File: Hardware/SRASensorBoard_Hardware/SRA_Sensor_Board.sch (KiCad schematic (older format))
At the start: 4 parts

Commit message: Added Okis to board
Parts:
- added C? (x4): CP1, symbol Device:CP1
- added C? (x2): C, symbol Device:C
- added D? (x2): LED, symbol Device:LED
- added J? (x2): Test_Point, symbol MRDT_Connectors:Test_Point
- added R? (x2): R, symbol Device:R
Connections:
- net at U?.1 (IN): now also C?.1 (x2)
- net at U?.2 (GND): now also C?.2, C?.2, C?.2 (x2)
- net at U?.3 (OUT): now also C?.1, C?.1, J?.1, R?.2 (x2)
- new net: D?.2 (A), R?.1 (x2)
- new net GND: D?.1 (K), D?.1 (K)
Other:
- moved on the sheet: Conn?A, Conn?B, U?

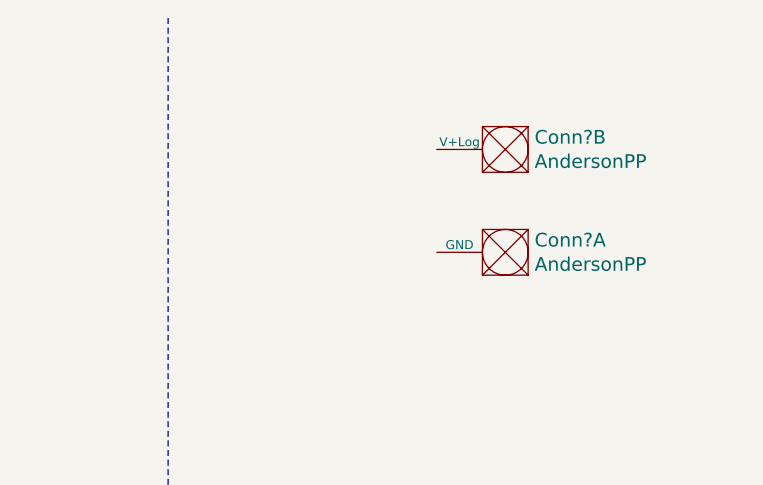
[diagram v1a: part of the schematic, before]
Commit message: Connected andersons 12v and gnd
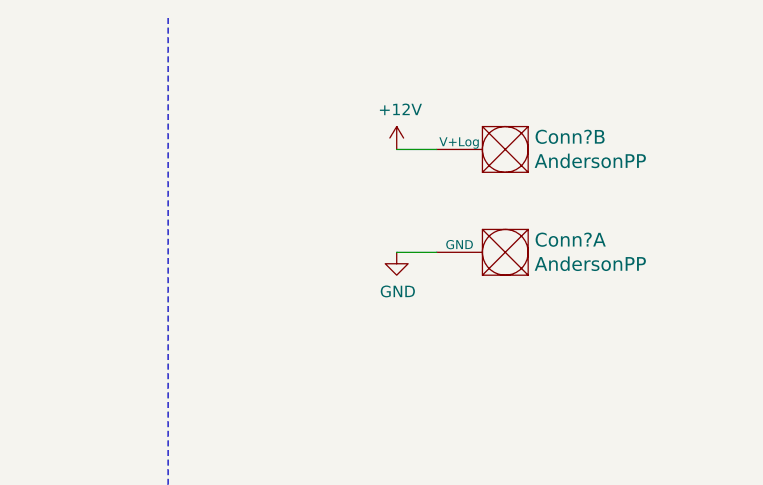
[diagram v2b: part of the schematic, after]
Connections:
- net GND: now also Conn?.1 (GND)
- net +12V: now reaches Conn?.2 (V+Log)
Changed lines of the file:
@@
 Wire Wire Line
 	9700 5225 10000 5225
+$Comp
+L power:+12V #PWR?
+U 1 1 615F977E
+P 9700 1050
+F 0 "#PWR?" H 9700 900 50  0001 C CNN
+F 1 "+12V" H 9715 1223 50  0000 C CNN
+F 2 "" H 9700 1050 50  0001 C CNN
+F 3 "" H 9700 1050 50  0001 C CNN
+	1    9700 1050
+	1    0    0    -1
+$EndComp
+$Comp
+L power:GND #PWR?
+U 1 1 615FA471
+P 9700 1500
+F 0 "#PWR?" H 9700 1250 50  0001 C CNN
+F 1 "GND" H 9705 1327 50  0000 C CNN
+F 2 "" H 9700 1500 50  0001 C CNN
+F 3 "" H 9700 1500 50  0001 C CNN
+	1    9700 1500
+	1    0    0    -1
+$EndComp
+Wire Wire Line
+	9700 1500 9875 1500
+Wire Wire Line
+	9875 1050 9700 1050
 $EndSCHEMATC

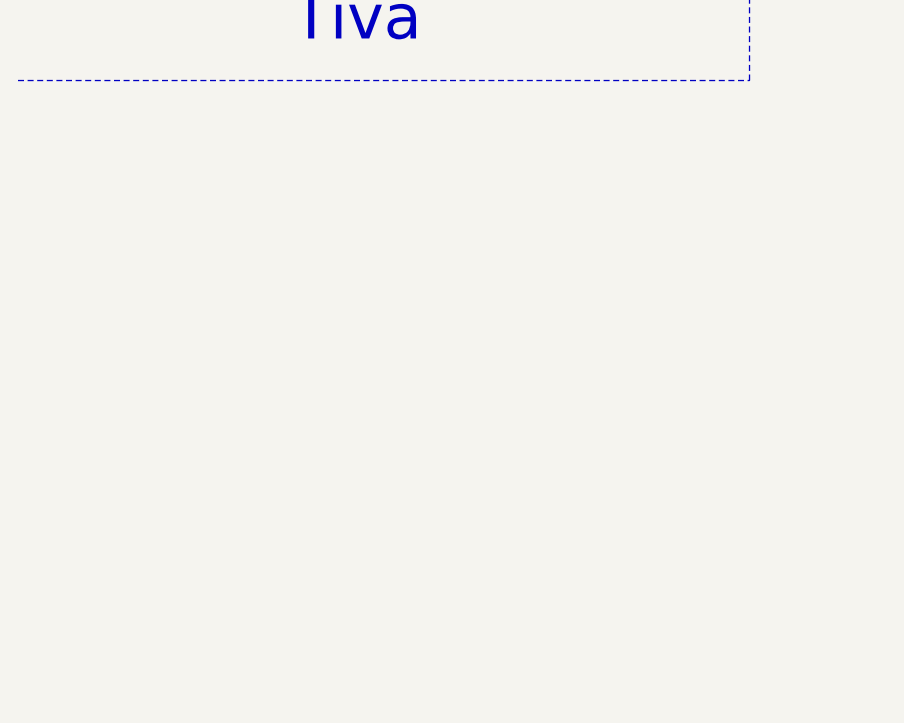
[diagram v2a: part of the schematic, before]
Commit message: Griffin_Buschjost_O2_Sensor
Copied in O2 Sensor from last year and added global labels to TIVA in pin 3 and 4 for the TIVA O2 RX and TX
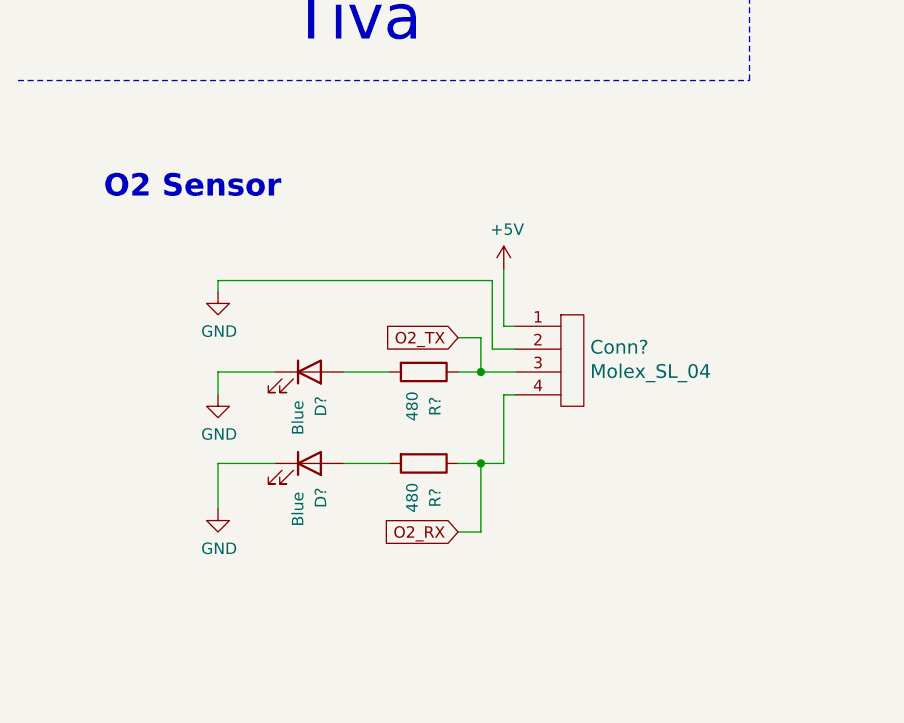
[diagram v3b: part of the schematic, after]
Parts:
- added Conn?: Molex_SL_04, symbol MRDT_Connectors:Molex_SL_04
- added D? (x2): Blue, symbol Device:LED
- added R? (x2): 480, symbol Device:R
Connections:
- net GND: now also Conn?.2, D?.1 (K), D?.1 (K)
- new net: D?.2 (A), R?.2 (x2)
- new net +5V: Conn?.1
- new net O2_RX: Conn?.4, R?.1
- new net O2_TX: Conn?.3, R?.1
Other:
- note added: "O2 Sensor"
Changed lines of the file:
@@
 Wire Wire Line
 	9875 1050 9700 1050
+$Comp
+L MRDT_Connectors:Molex_SL_04 Conn?
+U 1 1 615E28BA
+P 2850 4900
+F 0 "Conn?" H 2978 5158 60  0000 L CNN
+F 1 "Molex_SL_04" H 2978 5052 60  0000 L CNN
+F 2 "" H 2850 4900 60  0001 C CNN
+F 3 "" H 2850 4900 60  0001 C CNN
+	1    2850 4900
+	1    0    0    -1
+$EndComp
+$Comp
+L power:+5V #PWR?
+U 1 1 615E34E6
+P 2600 4300
+F 0 "#PWR?" H 2600 4150 50  0001 C CNN
+F 1 "+5V" H 2615 4473 50  0000 C CNN
+F 2 "" H 2600 4300 50  0001 C CNN
+F 3 "" H 2600 4300 50  0001 C CNN
+	1    2600 4300
+	1    0    0    -1
+$EndComp
+$Comp
+L power:GND #PWR?
+U 1 1 615E3C3C
+P 1350 4400
+F 0 "#PWR?" H 1350 4150 50  0001 C CNN
+F 1 "GND" H 1355 4227 50  0000 C CNN
+F 2 "" H 1350 4400 50  0001 C CNN
+F 3 "" H 1350 4400 50  0001 C CNN
+	1    1350 4400
+	1    0    0    -1
+$EndComp
+$Comp
+L Device:R R?
+U 1 1 615E564A
+P 2250 4750
+F 0 "R?" H 2400 4800 50  0000 C CNN
+F 1 "480" H 2400 4700 50  0000 C CNN
+F 2 "" V 2180 4750 50  0001 C CNN
+F 3 "~" H 2250 4750 50  0001 C CNN
+	1    2250 4750
+	0    1    1    0
+$EndComp
+$Comp
+L Device:R R?
+U 1 1 615E6832
+P 2250 5150
+F 0 "R?" H 2400 5200 50  0000 C CNN
+F 1 "480" H 2400 5100 50  0000 C CNN
+F 2 "" V 2180 5150 50  0001 C CNN
+F 3 "~" H 2250 5150 50  0001 C CNN
+	1    2250 5150
+	0    1    1    0
+$EndComp
+Wire Wire Line
+	2650 4550 2600 4550
+Wire Wire Line
+	2600 4550 2600 4300
+Wire Wire Line
+	2650 4650 2550 4650
+Wire Wire Line
+	2550 4650 2550 4350
+Wire Wire Line
+	2400 4750 2500 4750
+Wire Wire Line
+	2650 4850 2600 4850
+Wire Wire Line
+	2600 4850 2600 5150
+Wire Wire Line
+	2600 5150 2500 5150
+Connection ~ 2500 5150
+Wire Wire Line
+	2500 5150 2400 5150
+Wire Wire Line
+	2500 4750 2500 4600
+Wire Wire Line
+	2500 4600 2400 4600
+Connection ~ 2500 4750
+Wire Wire Line
+	2500 4750 2650 4750
+Text GLabel 2400 4600 0    50   Input ~ 0
+O2_TX
+Wire Wire Line
+	2100 4750 1900 4750
+Wire Wire Line
+	2100 5150 1900 5150
+$Comp
+L Device:LED D?
+U 1 1 615F2521
+P 1750 4750
+F 0 "D?" V 1800 4600 50  0000 C CNN
+F 1 "Blue" V 1700 4550 50  0000 C CNN
+F 2 "" H 1750 4750 50  0001 C CNN
+F 3 "~" H 1750 4750 50  0001 C CNN
+	1    1750 4750
+	1    0    0    -1
+$EndComp
+$Comp
+L Device:LED D?
+U 1 1 615F31B4
+P 1750 5150
+F 0 "D?" V 1800 5000 50  0000 C CNN
+F 1 "Blue" V 1700 4950 50  0000 C CNN
+F 2 "" H 1750 5150 50  0001 C CNN
+F 3 "~" H 1750 5150 50  0001 C CNN
+	1    1750 5150
+	1    0    0    -1
+$EndComp
+Wire Wire Line
+	1350 4750 1600 4750
+Wire Wire Line
+	1600 5150 1350 5150
+Wire Wire Line
+	1350 5150 1350 5350
+$Comp
+L power:GND #PWR?
+U 1 1 615F9848
+P 1350 4850
+F 0 "#PWR?" H 1350 4600 50  0001 C CNN
+F 1 "GND" H 1355 4677 50  0000 C CNN
+F 2 "" H 1350 4850 50  0001 C CNN
+F 3 "" H 1350 4850 50  0001 C CNN
+	1    1350 4850
+	1    0    0    -1
+$EndComp
+$Comp
+L power:GND #PWR?
+U 1 1 615FAB5A
+P 1350 5350
+F 0 "#PWR?" H 1350 5100 50  0001 C CNN
+F 1 "GND" H 1355 5177 50  0000 C CNN
+F 2 "" H 1350 5350 50  0001 C CNN
+F 3 "" H 1350 5350 50  0001 C CNN
+	1    1350 5350
+	1    0    0    -1
+$EndComp
+Wire Wire Line
+	1350 4750 1350 4850
+Wire Wire Line
+	2500 5450 2400 5450
+Wire Wire Line
+	2500 5150 2500 5450
+Text GLabel 2400 5450 0    50   Input ~ 0
+O2_RX
+Wire Wire Line
+	1350 4350 1350 4400
+Wire Wire Line
+	1350 4350 2550 4350
+Text Notes 850  4000 0    98   ~ 20
+O2 Sensor
 $EndSCHEMATC

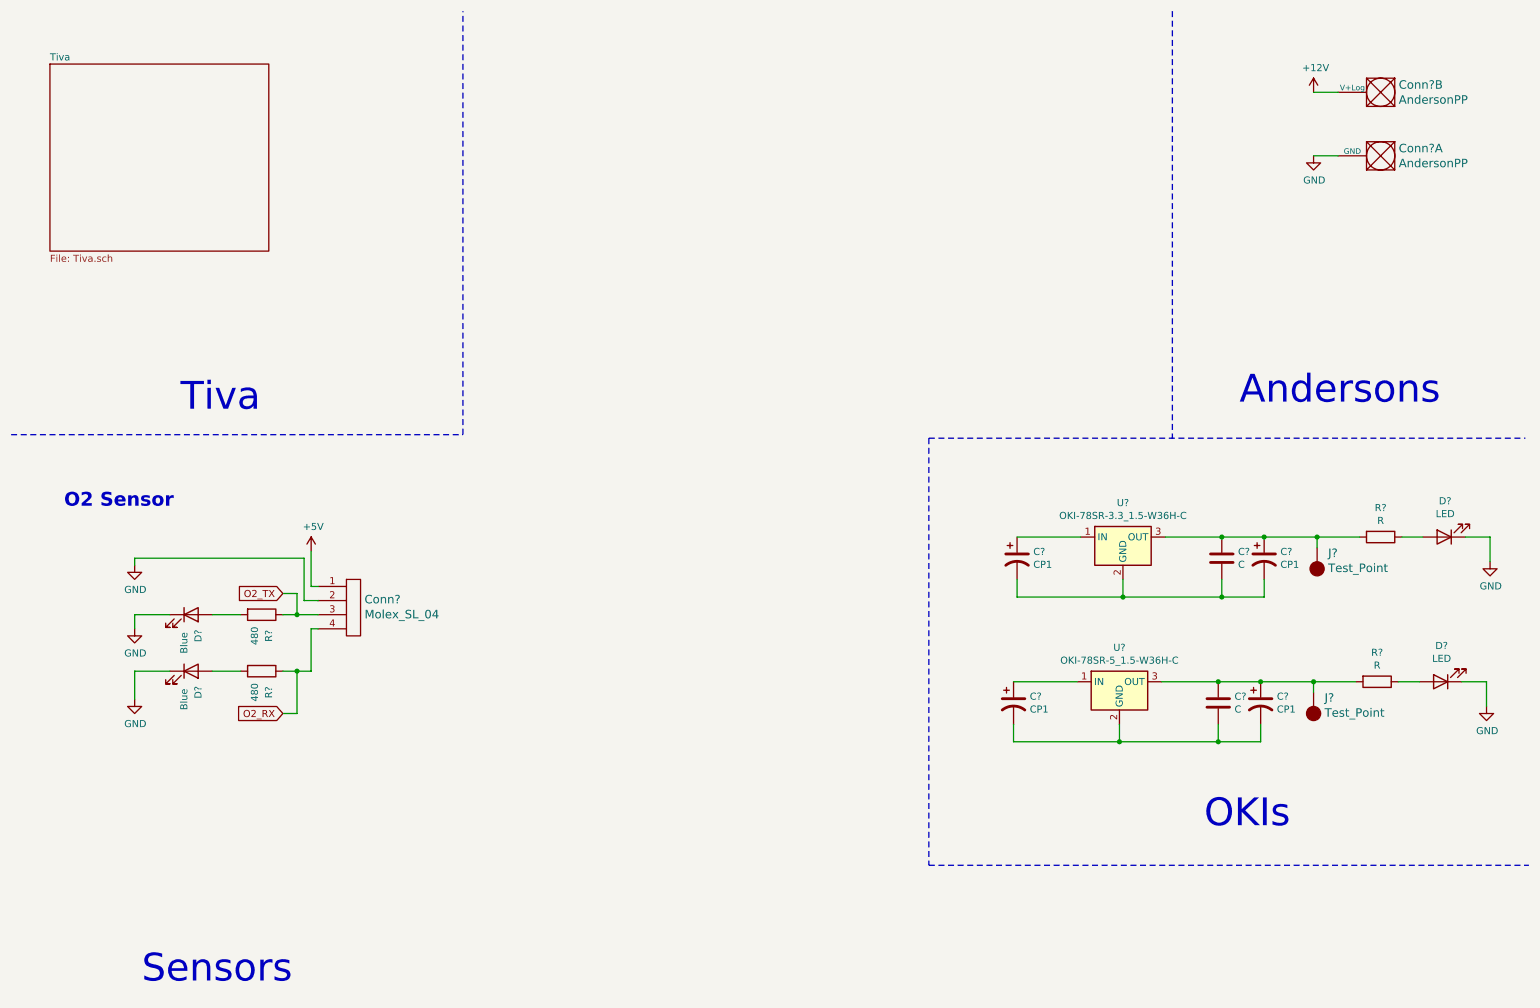
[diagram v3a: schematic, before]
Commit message: added CO2 sensor and fixed OKIs
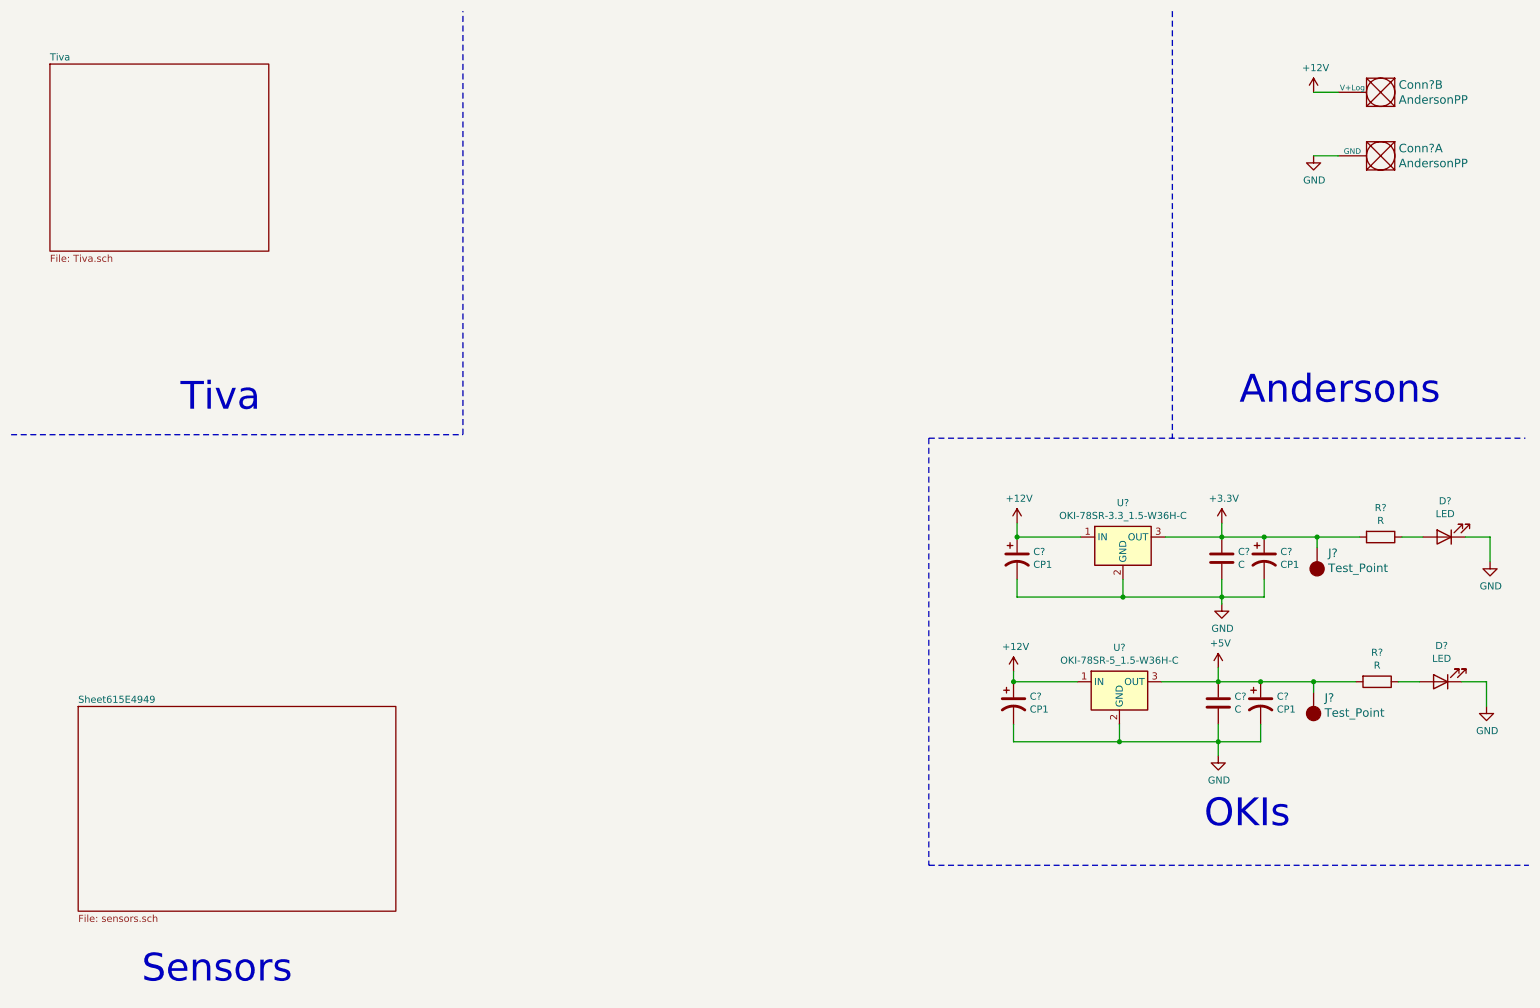
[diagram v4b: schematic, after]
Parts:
- removed Conn?: Molex_SL_04, symbol MRDT_Connectors:Molex_SL_04
- removed D? (x2): Blue, symbol Device:LED
- removed R? (x2): 480, symbol Device:R
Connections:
- net +12V: now also C?.1, C?.1, U?.1 (IN), U?.1 (IN)
- net +5V: now also C?.1, C?.1, J?.1, R?.2, U?.3 (OUT)
- net GND: now also C?.2, C?.2, C?.2, C?.2, C?.2, C?.2, U?.2 (GND), U?.2 (GND)
- net +3V3: now reaches C?.1, C?.1, J?.1, R?.2, U?.3 (OUT)
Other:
- note removed: "O2 Sensor"
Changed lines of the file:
@@
 $Descr A4 11693 8268
 encoding utf-8
-Sheet 1 2
+Sheet 1 3
 Title ""
 Date ""
@@
 Wire Wire Line
 	9875 1050 9700 1050
-$Comp
-L MRDT_Connectors:Molex_SL_04 Conn?
-U 1 1 615E28BA
-P 2850 4900
-F 0 "Conn?" H 2978 5158 60  0000 L CNN
-F 1 "Molex_SL_04" H 2978 5052 60  0000 L CNN
-F 2 "" H 2850 4900 60  0001 C CNN
-F 3 "" H 2850 4900 60  0001 C CNN
-	1    2850 4900
-	1    0    0    -1
-$EndComp
+$Sheet
+S 950  5400 2250 1450
+U 615E494A
+F0 "Sheet615E4949" 50
+F1 "sensors.sch" 50
+$EndSheet
+$Comp
+L power:+12V #PWR?
+U 1 1 615EE1DD
+P 7600 4100
+F 0 "#PWR?" H 7600 3950 50  0001 C CNN
+F 1 "+12V" H 7615 4273 50  0000 C CNN
+F 2 "" H 7600 4100 50  0001 C CNN
+F 3 "" H 7600 4100 50  0001 C CNN
+	1    7600 4100
+	1    0    0    -1
+$EndComp
+$Comp
+L power:+12V #PWR?
+U 1 1 615EEAA7
+P 7575 5150
+F 0 "#PWR?" H 7575 5000 50  0001 C CNN
+F 1 "+12V" H 7590 5323 50  0000 C CNN
+F 2 "" H 7575 5150 50  0001 C CNN
+F 3 "" H 7575 5150 50  0001 C CNN
+	1    7575 5150
+	1    0    0    -1
+$EndComp
+Wire Wire Line
+	7575 5225 7575 5150
+Connection ~ 7575 5225
+Wire Wire Line
+	7600 4200 7600 4100
+Connection ~ 7600 4200
 $Comp
 L power:+5V #PWR?
-U 1 1 615E34E6
-P 2600 4300
-F 0 "#PWR?" H 2600 4150 50  0001 C CNN
-F 1 "+5V" H 2615 4473 50  0000 C CNN
-F 2 "" H 2600 4300 50  0001 C CNN
-F 3 "" H 2600 4300 50  0001 C CNN
-	1    2600 4300
-	1    0    0    -1
-$EndComp
+U 1 1 615F1C53
+P 9025 5125
+F 0 "#PWR?" H 9025 4975 50  0001 C CNN
+F 1 "+5V" H 9040 5298 50  0000 C CNN
+F 2 "" H 9025 5125 50  0001 C CNN
+F 3 "" H 9025 5125 50  0001 C CNN
+	1    9025 5125
+	1    0    0    -1
+$EndComp
+Wire Wire Line
+	9025 5225 9025 5125
+$Comp
+L power:+3.3V #PWR?
+U 1 1 615F3DA4
+P 9050 4100
+F 0 "#PWR?" H 9050 3950 50  0001 C CNN
+F 1 "+3.3V" H 9065 4273 50  0000 C CNN
+F 2 "" H 9050 4100 50  0001 C CNN
+F 3 "" H 9050 4100 50  0001 C CNN
+	1    9050 4100
+	1    0    0    -1
+$EndComp
+Wire Wire Line
+	9050 4200 9050 4100
 $Comp
 L power:GND #PWR?
-U 1 1 615E3C3C
-P 1350 4400
-F 0 "#PWR?" H 1350 4150 50  0001 C CNN
-F 1 "GND" H 1355 4227 50  0000 C CNN
-F 2 "" H 1350 4400 50  0001 C CNN
-F 3 "" H 1350 4400 50  0001 C CNN
-	1    1350 4400
-	1    0    0    -1
-$EndComp
-$Comp
-L Device:R R?
-U 1 1 615E564A
-P 2250 4750
-F 0 "R?" H 2400 4800 50  0000 C CNN
-F 1 "480" H 2400 4700 50  0000 C CNN
-F 2 "" V 2180 4750 50  0001 C CNN
-F 3 "~" H 2250 4750 50  0001 C CNN
-	1    2250 4750
-	0    1    1    0
-$EndComp
-$Comp
-L Device:R R?
-U 1 1 615E6832
-P 2250 5150
-F 0 "R?" H 2400 5200 50  0000 C CNN
-F 1 "480" H 2400 5100 50  0000 C CNN
-F 2 "" V 2180 5150 50  0001 C CNN
-F 3 "~" H 2250 5150 50  0001 C CNN
-	1    2250 5150
-	0    1    1    0
-$EndComp
-Wire Wire Line
-	2650 4550 2600 4550
-Wire Wire Line
-	2600 4550 2600 4300
-Wire Wire Line
-	2650 4650 2550 4650
-Wire Wire Line
-	2550 4650 2550 4350
-Wire Wire Line
-	2400 4750 2500 4750
-Wire Wire Line
-	2650 4850 2600 4850
-Wire Wire Line
-	2600 4850 2600 5150
-Wire Wire Line
-	2600 5150 2500 5150
-Connection ~ 2500 5150
-Wire Wire Line
-	2500 5150 2400 5150
-Wire Wire Line
-	2500 4750 2500 4600
-Wire Wire Line
-	2500 4600 2400 4600
-Connection ~ 2500 4750
-Wire Wire Line
-	2500 4750 2650 4750
-Text GLabel 2400 4600 0    50   Input ~ 0
-O2_TX
-Wire Wire Line
-	2100 4750 1900 4750
-Wire Wire Line
-	2100 5150 1900 5150
-$Comp
-L Device:LED D?
-U 1 1 615F2521
-P 1750 4750
-F 0 "D?" V 1800 4600 50  0000 C CNN
-F 1 "Blue" V 1700 4550 50  0000 C CNN
-F 2 "" H 1750 4750 50  0001 C CNN
-F 3 "~" H 1750 4750 50  0001 C CNN
-	1    1750 4750
-	1    0    0    -1
-$EndComp
-$Comp
-L Device:LED D?
-U 1 1 615F31B4
-P 1750 5150
-F 0 "D?" V 1800 5000 50  0000 C CNN
-F 1 "Blue" V 1700 4950 50  0000 C CNN
-F 2 "" H 1750 5150 50  0001 C CNN
-F 3 "~" H 1750 5150 50  0001 C CNN
-	1    1750 5150
-	1    0    0    -1
-$EndComp
-Wire Wire Line
-	1350 4750 1600 4750
-Wire Wire Line
-	1600 5150 1350 5150
-Wire Wire Line
-	1350 5150 1350 5350
+U 1 1 615F5CA8
+P 9025 5750
+F 0 "#PWR?" H 9025 5500 50  0001 C CNN
+F 1 "GND" H 9030 5577 50  0000 C CNN
+F 2 "" H 9025 5750 50  0001 C CNN
+F 3 "" H 9025 5750 50  0001 C CNN
+	1    9025 5750
+	1    0    0    -1
+$EndComp
+Wire Wire Line
+	9025 5750 9025 5650
 $Comp
 L power:GND #PWR?
-U 1 1 615F9848
-P 1350 4850
-F 0 "#PWR?" H 1350 4600 50  0001 C CNN
-F 1 "GND" H 1355 4677 50  0000 C CNN
-F 2 "" H 1350 4850 50  0001 C CNN
-F 3 "" H 1350 4850 50  0001 C CNN
-	1    1350 4850
-	1    0    0    -1
-$EndComp
-$Comp
-L power:GND #PWR?
-U 1 1 615FAB5A
-P 1350 5350
-F 0 "#PWR?" H 1350 5100 50  0001 C CNN
-F 1 "GND" H 1355 5177 50  0000 C CNN
-F 2 "" H 1350 5350 50  0001 C CNN
-F 3 "" H 1350 5350 50  0001 C CNN
-	1    1350 5350
-	1    0    0    -1
-$EndComp
-Wire Wire Line
-	1350 4750 1350 4850
-Wire Wire Line
-	2500 5450 2400 5450
-Wire Wire Line
-	2500 5150 2500 5450
-Text GLabel 2400 5450 0    50   Input ~ 0
-O2_RX
-Wire Wire Line
-	1350 4350 1350 4400
-Wire Wire Line
-	1350 4350 2550 4350
-Text Notes 850  4000 0    98   ~ 20
-O2 Sensor
+U 1 1 615F72EB
+P 9050 4675
+F 0 "#PWR?" H 9050 4425 50  0001 C CNN
+F 1 "GND" H 9055 4502 50  0000 C CNN
+F 2 "" H 9050 4675 50  0001 C CNN
+F 3 "" H 9050 4675 50  0001 C CNN
+	1    9050 4675
+	1    0    0    -1
+$EndComp
+Wire Wire Line
+	9050 4675 9050 4625
 $EndSCHEMATC
